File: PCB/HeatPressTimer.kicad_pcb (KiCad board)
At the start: 2 copper layers, 58 x 35 mm, 6 parts, among them J1 2" SPI ST7789VW Display, J2 Piezo, SW1 Switch, SW2 Switch, SW3 Vertical Limit Switch, U1 XIAO-ESP32-C6

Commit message: new PCB files
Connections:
- U1 pad 5: unconnected-(U1-GPIO22/D4/SDA-Pad5) -> PIEZO
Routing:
- net PIEZO: track 0.00 -> 23.8 mm, vias 0 -> 2
- net unconnected-(U1-GPIO22/D4/SDA-Pad5): track 0.83 -> 0.00 mm
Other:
- board text added: "luteron6 heatpress-timer v2 6.23.2025"
- board text removed: "luteron6 heatpress-timer v1 5.23.2025"
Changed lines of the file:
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@@
 	(net 13 "unconnected-(U1-VBUS-Pad14)")
 	(net 14 "unconnected-(U1-GPIO0{slash}A0{slash}D0-Pad1)")
-	(net 15 "unconnected-(U1-GPIO22{slash}D4{slash}SDA-Pad5)")
 	(footprint "custom-library:2-pin pads"
 		(layer "F.Cu")
@@
 			(at 0 -14.2 0)
 			(unlocked yes)
-			(layer "F.SilkS")
+			(layer "F.Fab")
 			(effects
 				(font
@@
 			(layers "F.Cu" "F.Mask")
 			(roundrect_rratio 0.1)
-			(net 15 "unconnected-(U1-GPIO22{slash}D4{slash}SDA-Pad5)")
+			(net 5 "PIEZO")
 			(pinfunction "GPIO22/D4/SDA")
 			(pintype "passive")
@@
 			(layers "*.Cu" "*.Mask")
 			(remove_unused_layers no)
-			(net 15 "unconnected-(U1-GPIO22{slash}D4{slash}SDA-Pad5)")
+			(net 5 "PIEZO")
 			(pinfunction "GPIO22/D4/SDA")
 			(pintype "passive")
@@
 		)
 	)
-	(gr_text "luteron6\nheatpress-timer v1\n5.23.2025"
-		(at 87.5 84 0)
+	(gr_text "luteron6\nheatpress-timer v2\n6.23.2025"
+		(at 70.240625 84 0)
 		(layer "F.SilkS")
 		(effects
 			(font
-				(size 1 1)
-				(thickness 0.15)
+				(size 2 2)
+				(thickness 0.25)
 			)
 			(justify left bottom)
@@
 	)
 	(segment
+		(start 63.0861 72.6269)
+		(end 63.0861 62.36735)
+		(width 0.2)
+		(layer "F.Cu")
+		(net 5)
+	)
+	(segment
+		(start 63.0861 62.36735)
+		(end 60.715625 59.996875)
+		(width 0.2)
+		(layer "F.Cu")
+		(net 5)
+	)
+	(segment
+		(start 63.0861 72.6269)
+		(end 63.0861 73.4619)
+		(width 0.2)
+		(layer "F.Cu")
+		(net 5)
+	)
+	(via
+		(at 60.715625 51.6625)
+		(size 0.6)
+		(drill 0.3)
+		(layers "F.Cu" "B.Cu")
+		(net 5)
+	)
+	(via
+		(at 60.715625 59.996875)
+		(size 0.6)
+		(drill 0.3)
+		(layers "F.Cu" "B.Cu")
+		(net 5)
+	)
+	(segment
+		(start 59.4841 52.894025)
+		(end 60.715625 51.6625)
+		(width 0.2)
+		(layer "B.Cu")
+		(net 5)
+	)
+	(segment
+		(start 60.715625 59.996875)
+		(end 59.4841 58.76535)
+		(width 0.2)
+		(layer "B.Cu")
+		(net 5)
+	)
+	(segment
+		(start 59.4841 58.76535)
+		(end 59.4841 52.894025)
+		(width 0.2)
+		(layer "B.Cu")
+		(net 5)
+	)
+	(segment
 		(start 82.0238 55.0238)
 		(end 93.5 66.5)
@@
 		(net 14)
 	)
-	(segment
-		(start 63.0861 72.6269)
-		(end 63.0861 73.4619)
-		(width 0.2)
-		(layer "F.Cu")
-		(net 15)
-	)
 )

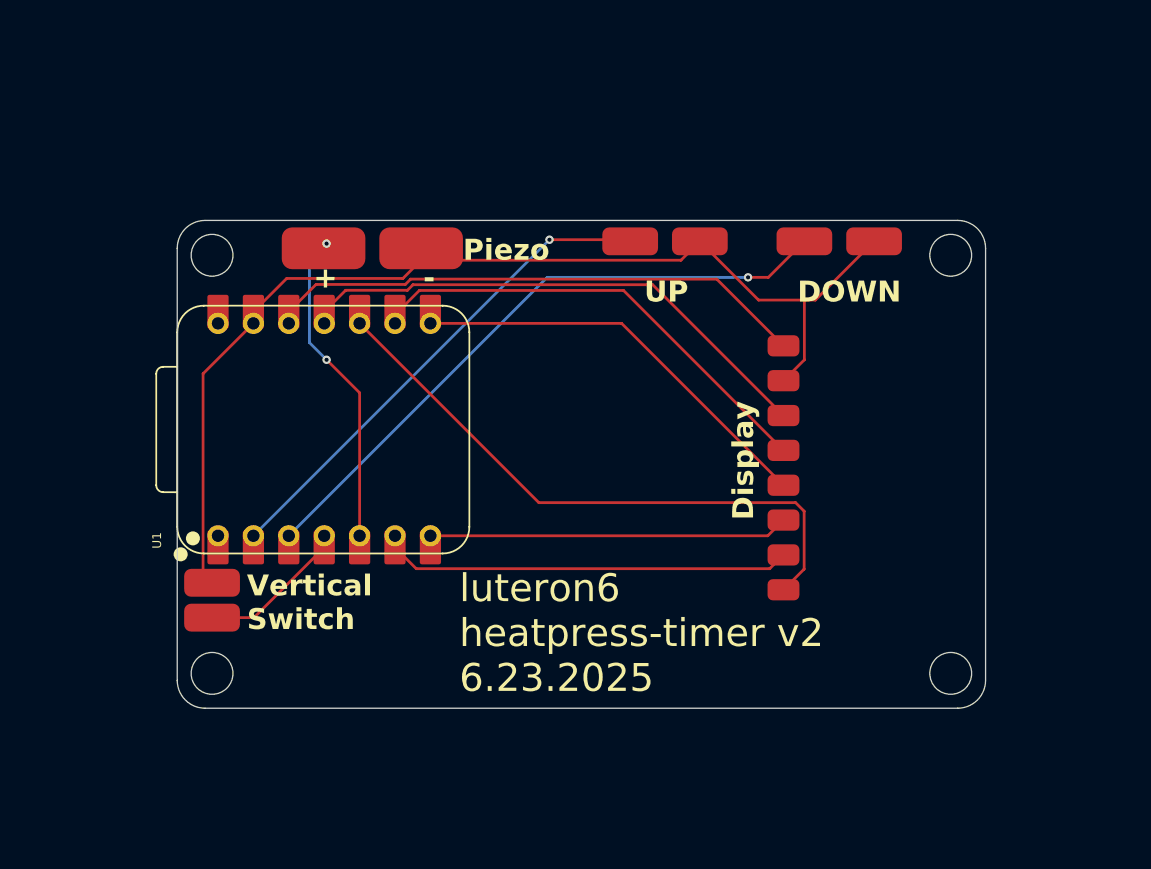
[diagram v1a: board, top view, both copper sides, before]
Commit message: Added filled zone to PCB
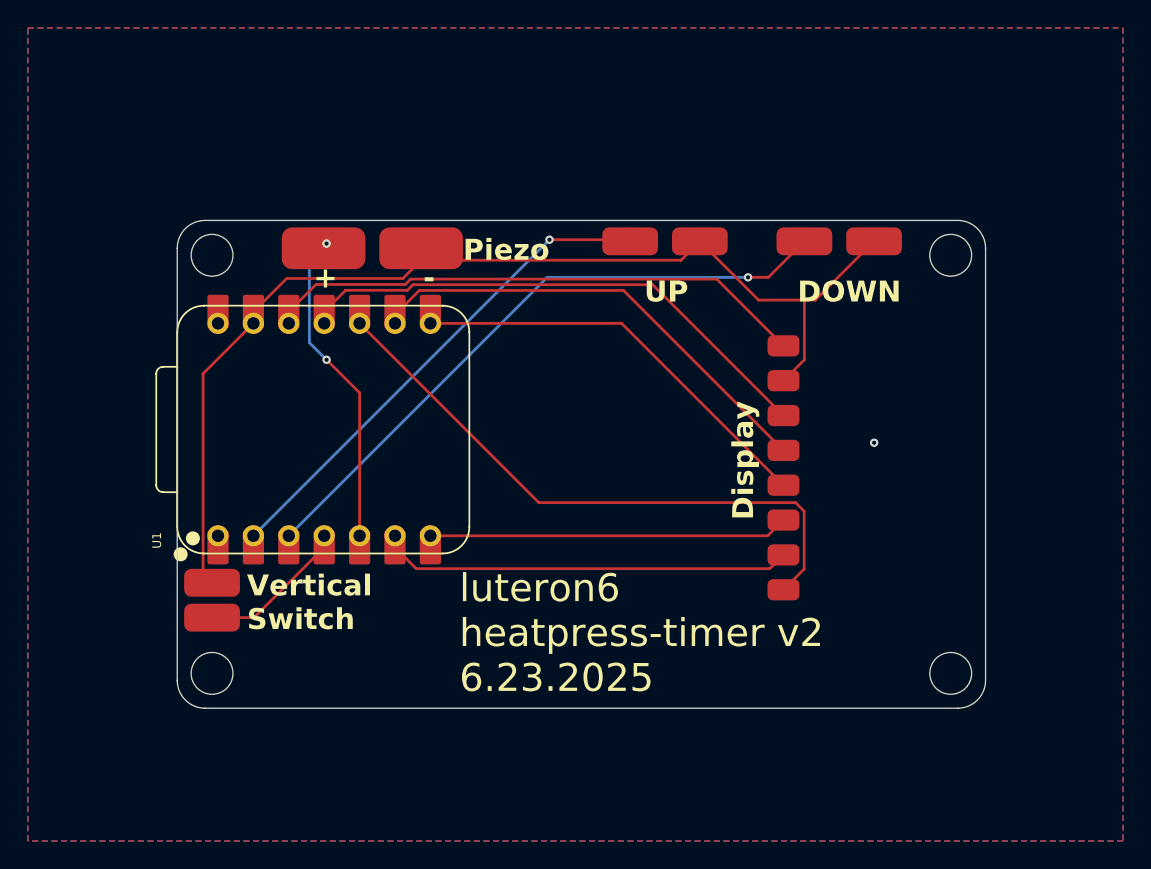
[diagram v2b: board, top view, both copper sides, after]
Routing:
- net GND: vias 0 -> 1
- added copper zone on B.Cu, net GND
- added copper zone on F.Cu, net GND
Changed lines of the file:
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@@
+		(net 2)
+	)
+	(via
+		(at 100.00625 65.95)
+		(size 0.6)
+		(drill 0.3)
+		(layers "F.Cu" "B.Cu")
+		(free yes)
 		(net 2)
 	)
@@
 		(net 14)
 	)
+	(zone
+		(net 2)
+		(net_name "GND")
+		(layers "F&B.Cu")
+		(hatch edge 0.5)
+		(connect_pads
+			(clearance 0.5)
+		)
+		(min_thickness 0.25)
+		(filled_areas_thickness no)
+		(fill yes
+			(thermal_gap 0.5)
+			(thermal_bridge_width 0.5)
+		)
+		(polygon
+			(pts
+				(xy 39.284375 36.184375) (xy 117.865625 36.184375) (xy 117.865625 94.525) (xy 39.284375 94.525)
+			)
+		)
+	)
 )
